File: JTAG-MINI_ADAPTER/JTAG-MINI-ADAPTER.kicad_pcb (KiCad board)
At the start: 2 copper layers, 21.4 x 46.5 mm, 2 parts, among them J1 ATMEL-ICE SAM SOCKET, J12 SWD/JTAG SAM (ARM/Cortex-M db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

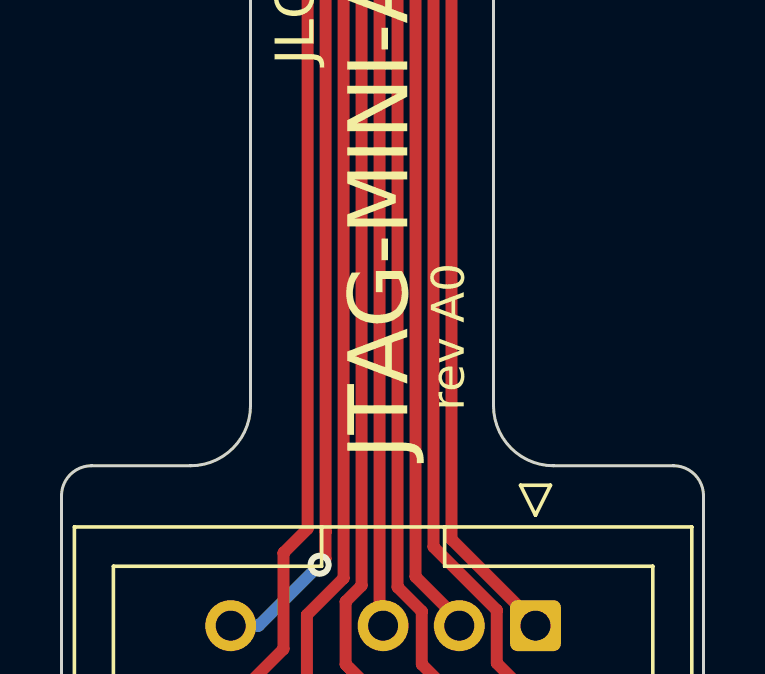
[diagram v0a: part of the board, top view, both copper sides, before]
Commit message: JTAG-MINI-ADAPTER: rev A1 - add OHL license and use kibot
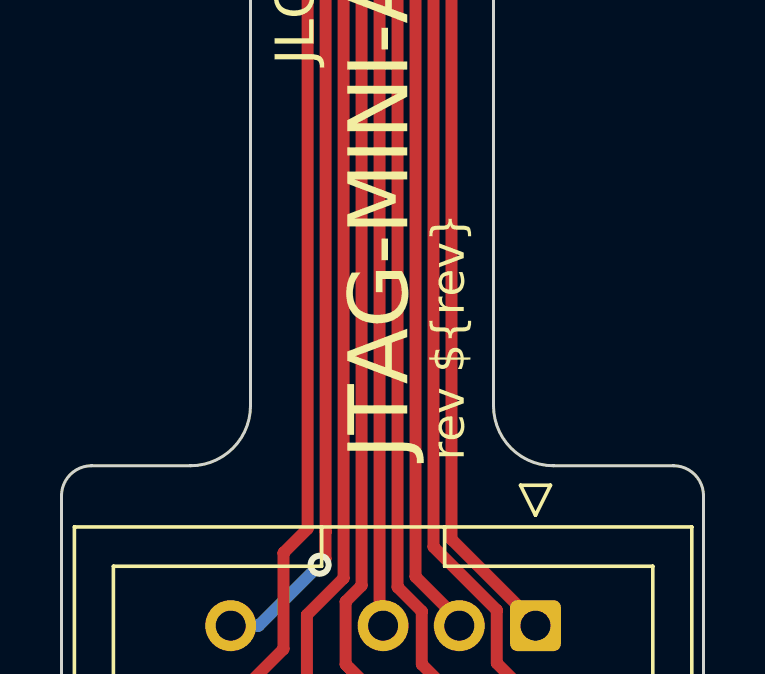
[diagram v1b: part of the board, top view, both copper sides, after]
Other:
- board text added: "${license}"
- board text added: "rev ${rev}"
- board text removed: "rev A0"
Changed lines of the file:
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@@
   )
   (paper "A4")
+  (title_block
+    (rev "${rev}")
+  )
   (layers
     (0 "F.Cu" signal)
@@
     )
   )
+  (property "license" "Licensed under CERN-OHL-W v2")
+  (property "rev" "A1")
   (net 0 "")
   (net 1 "unconnected-(J1-Pad7)")
@@
   (gr_arc (start 94.699997 143.499997) (mid 93.992891 143.207103) (end 93.699997 142.499997) (layer "Edge.Cuts") (width 0.1))
   (gr_arc (start 110.099999 131.499999) (mid 108.685785 130.914213) (end 108.099999 129.499999) (layer "Edge.Cuts") (width 0.1))
+  (gr_text "${license}" (at 104.36 118.85 -90) (layer "B.SilkS")
+    (effects (font (size 1.3 1.3) (thickness 0.18)) (justify mirror))
+  )
   (gr_text "JTAG-MINI-ADAPTER" (at 104.3 117.6 90) (layer "F.SilkS")
     (effects (font (size 2 2) (thickness 0.25)))
   )
-  (gr_text "rev A0" (at 106.6 127.2 90) (layer "F.SilkS")
+  (gr_text "rev ${rev}" (at 106.6 127.2 90) (layer "F.SilkS")
     (effects (font (size 1.1 1.1) (thickness 0.154)))
   )
